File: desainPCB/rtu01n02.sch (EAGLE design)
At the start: 12 parts, among them M1 ARDUINO-PRO-MINI-5.0V, U1 GY-521MPU6050, X1 JST-XH-02-PIN-LONG-PAD

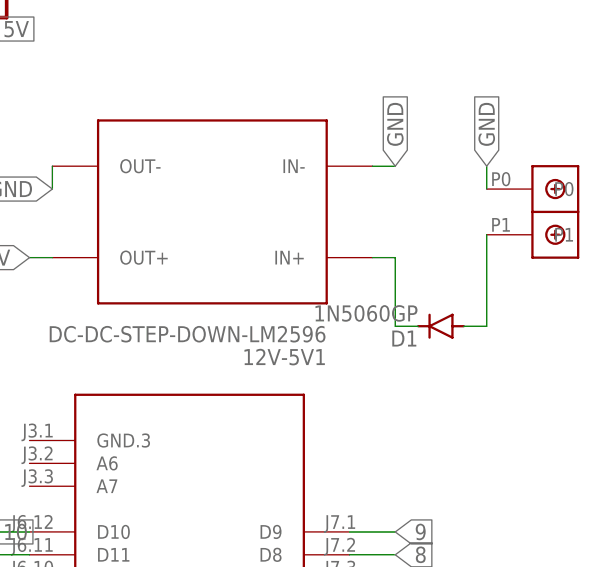
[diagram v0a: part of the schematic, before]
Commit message: new sensor suhu
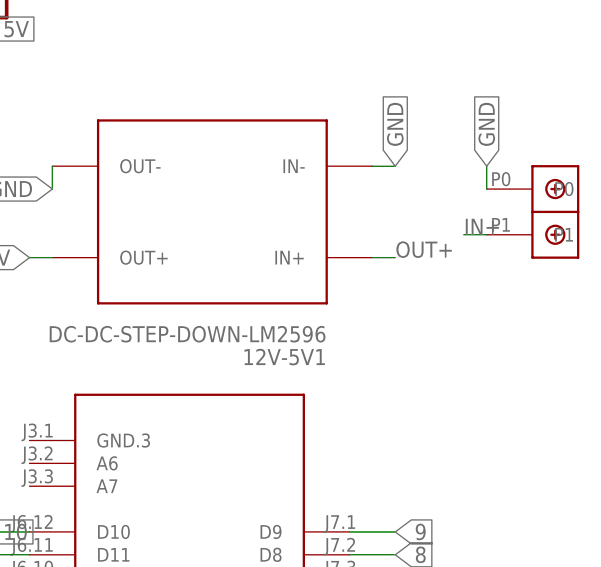
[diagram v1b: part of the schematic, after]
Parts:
- removed D1: 1N5060GP, diode:1N5060GP
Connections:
- removed net N$1: D1.A, U$1.P1
- removed net N$2: 12V-5V1.IN+, D1.C
- new net IN+: U$1.P1
- new net OUT+: 12V-5V1.IN+
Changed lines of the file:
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@@
 <part name="MICRO" library="pinhead" library_urn="urn:adsk.eagle:library:325" deviceset="PINHD-1X2" device="" package3d_urn="urn:adsk.eagle:package:22435/2"/>
 <part name="USB" library="pinhead" library_urn="urn:adsk.eagle:library:325" deviceset="PINHD-1X2" device="" package3d_urn="urn:adsk.eagle:package:22435/2"/>
-<part name="D1" library="diode" library_urn="urn:adsk.eagle:library:210" deviceset="1N5060GP" device="" package3d_urn="urn:adsk.eagle:package:43369/2"/>
 </parts>
 <sheets>
@@
 <attribute name="VALUE" x="-1.27" y="109.22" size="1.778" layer="96" rot="R180"/>
 </instance>
-<instance part="D1" gate="1" x="93.98" y="68.58" smashed="yes" rot="R180">
-<attribute name="NAME" x="91.44" y="68.0974" size="1.778" layer="95" rot="R180"/>
-<attribute name="VALUE" x="91.44" y="70.8914" size="1.778" layer="96" rot="R180"/>
-</instance>
 </instances>
 <busses>
@@
 </segment>
 </net>
-<net name="N$1" class="0">
-<segment>
-<pinref part="U$1" gate="G$1" pin="P1"/>
-<wire x1="99.06" y1="78.74" x2="99.06" y2="68.58" width="0.1524" layer="91"/>
-<pinref part="D1" gate="1" pin="A"/>
-<wire x1="99.06" y1="68.58" x2="96.52" y2="68.58" width="0.1524" layer="91"/>
-</segment>
-</net>
-<net name="N$2" class="0">
-<segment>
-<pinref part="D1" gate="1" pin="C"/>
-<wire x1="91.44" y1="68.58" x2="88.9" y2="68.58" width="0.1524" layer="91"/>
-<wire x1="88.9" y1="68.58" x2="88.9" y2="76.2" width="0.1524" layer="91"/>
+<net name="OUT+" class="0">
+<segment>
 <pinref part="12V-5V1" gate="G$1" pin="IN+"/>
 <wire x1="88.9" y1="76.2" x2="86.36" y2="76.2" width="0.1524" layer="91"/>
-</segment>
-</net>
+<label x="88.9" y="76.2" size="1.778" layer="95"/>
+</segment>
+</net>
+<net name="IN+" class="0">
+<segment>
+<pinref part="U$1" gate="G$1" pin="P1"/>
+<wire x1="99.06" y1="78.74" x2="96.52" y2="78.74" width="0.1524" layer="91"/>
+<label x="96.52" y="78.74" size="1.778" layer="95"/>
+</segment>
+</net>
